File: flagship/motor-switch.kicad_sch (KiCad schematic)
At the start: 21 parts, among them J2 BUS_OUT, Q401 PSMN3R7-100BSE, Q402 PSMN3R7-100BSE, Q403 DMN10H220L, Q404 MMBT3904, U2 TPS48111

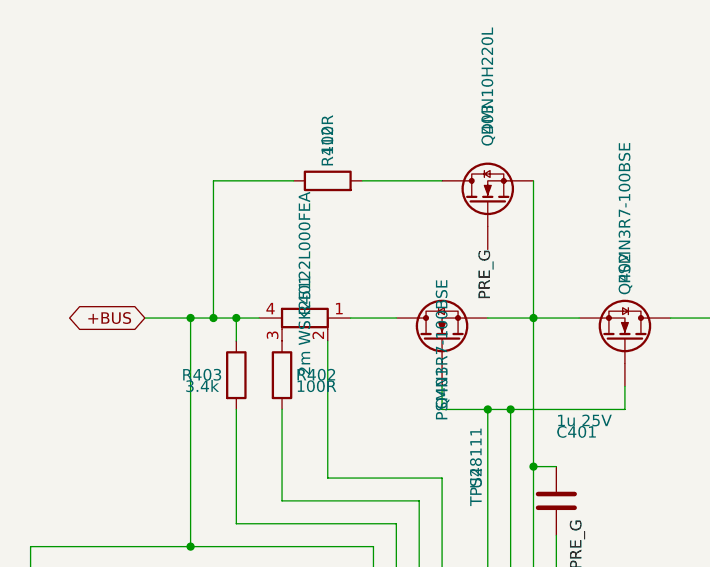
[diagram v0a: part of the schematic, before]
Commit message: flagship: shunts to LCSC stock -- WSK1216 true Kelvin for the INA228, CSS2H 2 mOhm pseudo-Kelvin (net-tied sense pads) for the LTC4364 and motor switch
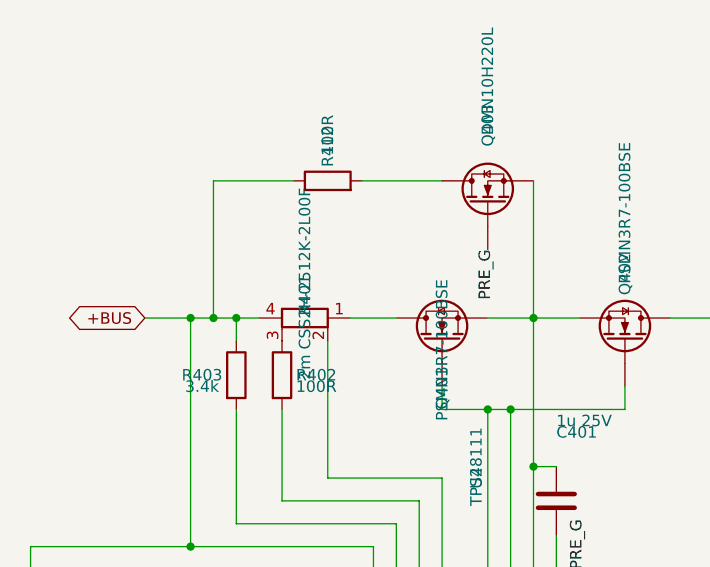
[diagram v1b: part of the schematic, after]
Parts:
- R401: value 2m WSK25122L000FEA -> 2m CSS2H-2512K-2L00F; footprint Resistor_SMD:R_Shunt_Vishay_WSK2512_6332Metric_T2.21mm -> flagship:R_2512_Shunt_PseudoKelvin
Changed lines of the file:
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@@
 			)
 		)
-		(property "Value" "2m WSK25122L000FEA"
+		(property "Value" "2m CSS2H-2512K-2L00F"
 			(at 43.18 57.15 0)
 			(show_name no)
@@
 			)
 		)
-		(property "Footprint" "Resistor_SMD:R_Shunt_Vishay_WSK2512_6332Metric_T2.21mm"
+		(property "Footprint" "flagship:R_2512_Shunt_PseudoKelvin"
 			(at 41.4 60.96 90)
 			(hide yes)
